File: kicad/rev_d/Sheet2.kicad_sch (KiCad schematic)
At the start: 212 parts, among them J10 vg_old, J5 external clock, J6 JUMPER, J8 JUMPER, J9 JUMPER, Q2 QUARTZ, Q3 QUARTZ32768, X10 ST-214C, X11 KEYB-MOUSE, X12 IDC20, X13 USB_C, X14 AAFP/AC97 audio, X15 PLB2-2, X16 PLB1-4I, X17 PLB1-4I, X18 PLB1-4I, X19 AVR pgm conn, X20 PLB1-4I, X21 RSA103, X4 IDC10M, X5 IDC10M, X6 RS232_9

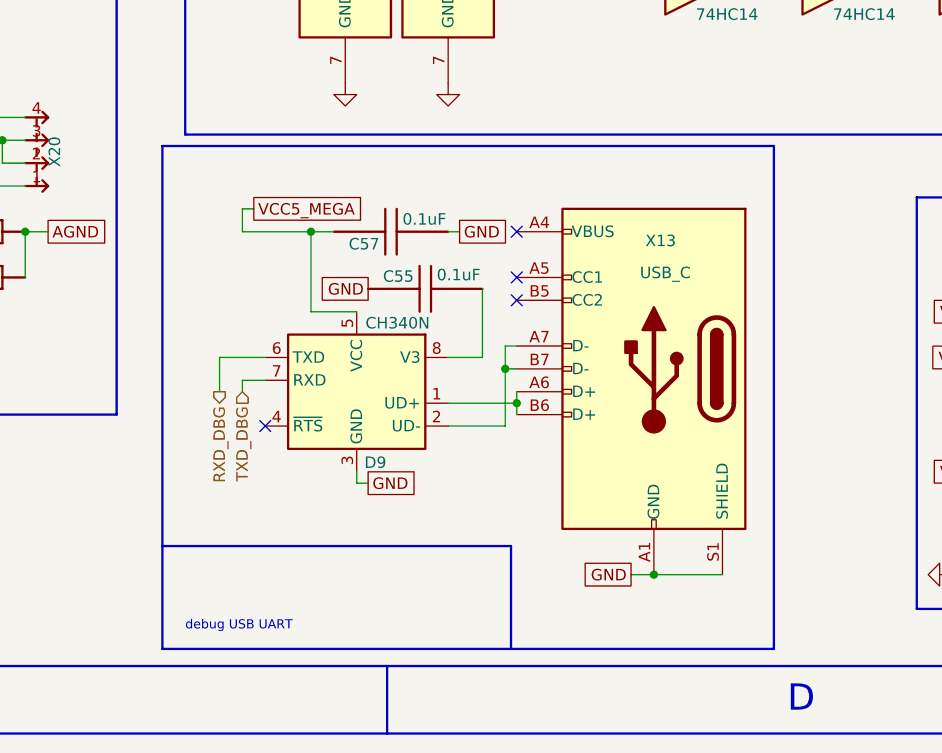
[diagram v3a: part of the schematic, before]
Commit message: pentevo: rev D: add forgotten 5k1 pulldowns for type-C CC1/CC2 pins
git-svn-id: svn://localhost/local-pentevo@1207 c6c76956-fad2-4150-a3a9-ea0a427205ba
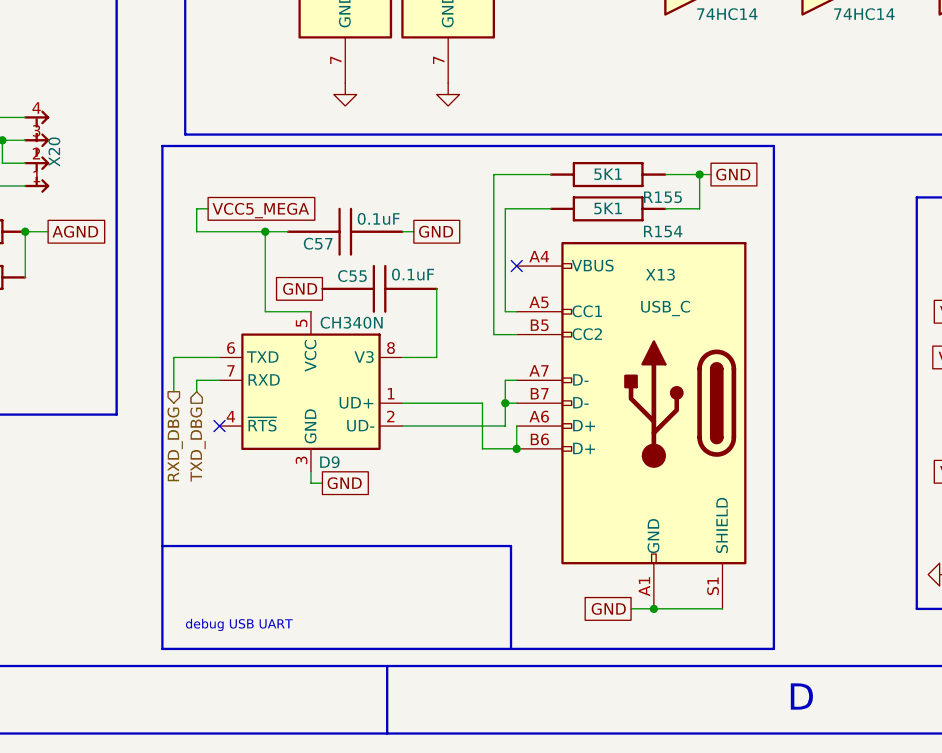
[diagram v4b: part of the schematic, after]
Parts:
- added R154, R155: 5K1, R-CHIP, symbol eva-altium-import:Sheet2_0_mirrored_RESCHIP
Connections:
- net GND: now also R154.2 (i/o1), R155.2 (i/o1)
- net at X13.A5 (CC1): now also R154.1 (i/o)
- net at X13.B5 (CC2): now also R155.1 (i/o)
- no-connect marks 31 -> 29
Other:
- moved on the sheet: C55, C57, D9, X13

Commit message: pentevo: rev D: upgrade 12v filtering, add 74hct1g04 for beep signals (much faster speed), change AVCC8 to AVCC9
git-svn-id: svn://localhost/local-pentevo@1209 c6c76956-fad2-4150-a3a9-ea0a427205ba
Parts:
- removed C12: 10uF, EC-CHIP, symbol eva-altium-import:Sheet2_3_ECAPCHIP
- removed D20: CD4069M, SO14, symbol eva-altium-import:Sheet2_0_CD4069M
- removed R99: 91, R-CHIP, symbol eva-altium-import:Sheet2_3_RESCHIP
- removed X21: RSA103, RSA103, symbol eva-altium-import:Sheet2_0_RSA103
- added C12: 0.1uF, C-CHIP, symbol eva-altium-import:Sheet2_0_CAPCHIP
- added C58, C63: 470uF, EC-CHIP, symbol eva-altium-import:Sheet2_3_ECAPCHIP
- added D20: 4069, Package_SO:SOIC-14_3.9x8.7mm_P1.27mm, symbol 4xxx:4069
- added L4: 470uH, CDR64B, symbol eva-altium-import:Sheet2_0_CDR64B
- added R156, R99: 0R5, R-CHIP, symbol eva-altium-import:Sheet2_0_RESCHIP
- added U1: 74HCT1G04, Package_TO_SOT_SMD:SOT-23-5_HandSoldering, symbol 74xGxx:74AHC1G04
- C44: value 10nF -> 1nF
- L2: value 27uH -> 470uH
- R114: value 2K2 -> 1K6
- R87: value 91 -> 150
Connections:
- net AGND: now also C44.1, C12.1, C58.2, C63.2, D20.7 (VSS), U1.3 (GND)
- net AVCC5: now also C12.2, D20.14 (VDD), U1.5 (VCC)
- net BEEP: now also D20.3, U1.2
- net TAPE_BIT: now also D20.8
- net at R95.1 (i/o): now also D20.10, D20.9
- net at C14.1, C15.1, DA2.1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: now also R87.1 (i/o)
- net at R164.2 (i/o1): now also D20.4
- net at R95.2 (i/o1), VD7.2 (C), VD8.1 (A): now also D20.11, D20.12
- net AVCC12: now reaches C10.1, C35.1, DA2.3 (in), DA5.1 (in), VD18.1 (K), VD19.1 (K)
- net AVCC12: now also C63.1, R156.2 (i/o1); no longer L2.1
- net at R94.1 (i/o), VD7.1 (A), VD8.2 (C): now also D20.13
- net at R114.2 (i/o1): now also U1.4
- net AVCC8 renamed AVCC9
- net AVCC9: no longer C44.1
- new net: C58.1, L4.1, R99.1 (i/o)
- new net: L2.1, R99.2 (i/o1)
- new net: D20.1, D20.6
- new net: D20.2, D20.5
- new net: L4.2, R156.1 (i/o)
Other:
- note added: "alt. supervisor is KA75450"
- moved on the sheet: C10, C105, C11, C13, C14, C15, C29, C33, C35, C37, DA2, R87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

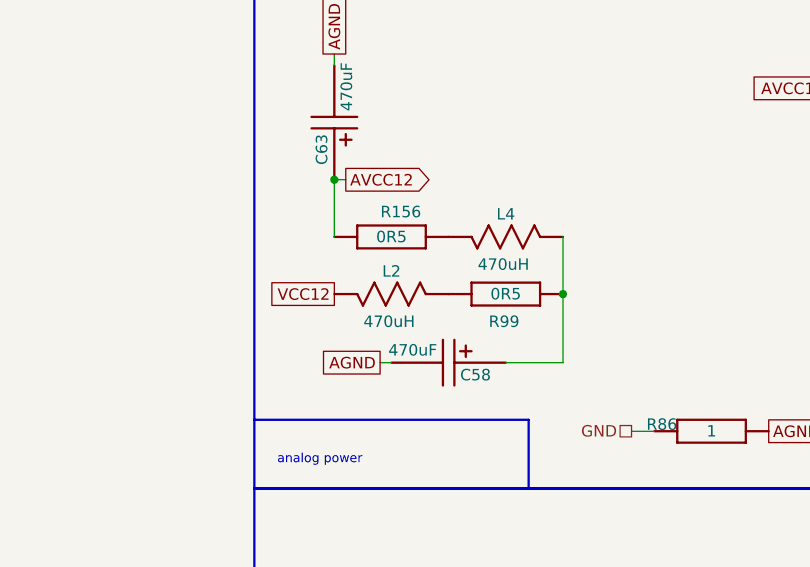
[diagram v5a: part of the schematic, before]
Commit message: pentevo: rev D: update footprints for 470uF and 470uH, remove 0R5 resistors
git-svn-id: svn://localhost/local-pentevo@1210 c6c76956-fad2-4150-a3a9-ea0a427205ba
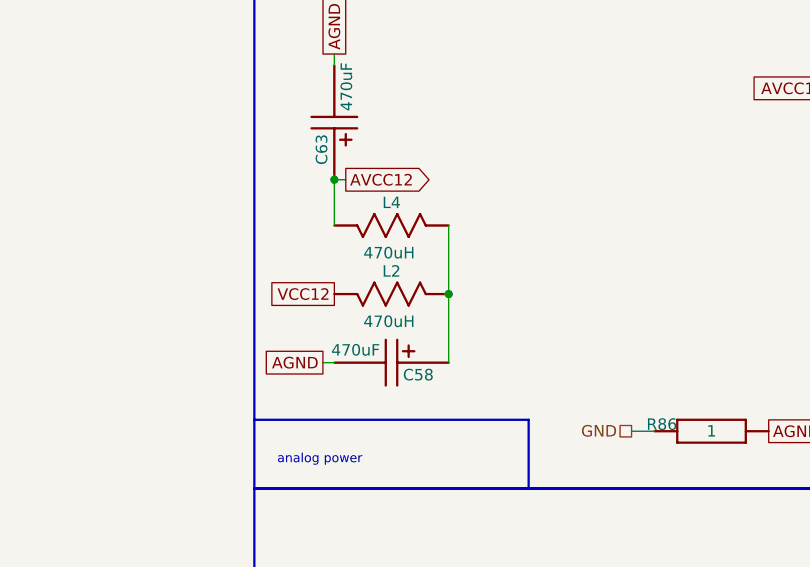
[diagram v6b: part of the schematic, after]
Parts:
- removed R156, R99: 0R5, R-CHIP, symbol eva-altium-import:Sheet2_0_RESCHIP
- C58, C63: footprint EC-CHIP -> Capacitor_THT:CP_Radial_D10.0mm_P5.00mm
- L2, L4: footprint CDR64B -> Inductor_SMD:L_Bourns_SRP6060FA
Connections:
- net AVCC12: now also L4.2
- net at C58.1, L4.1: now also L2.1
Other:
- moved on the sheet: C58, L4
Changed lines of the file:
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@@
 	)
 	(junction
-		(at 115.57 257.81)
-		(diameter 0)
-		(color 0 0 0 0)
-	)
-	(junction
 		(at 384.81 85.09)
 		(diameter 0)
@@
 	)
 	(junction
+		(at 102.87 257.81)
+		(diameter 0)
+		(color 0 0 0 0)
+	)
+	(junction
 		(at 147.32 335.28)
 		(diameter 0)
@@
 	(wire
 		(pts
+			(xy 102.87 250.19) (xy 102.87 257.81)
+		)
+		(stroke
+			(width 0)
+			(type default)
+		)
+	)
+	(wire
+		(pts
 			(xy 297.18 195.58) (xy 330.2 195.58)
 		)
@@
 	(wire
 		(pts
-			(xy 115.57 265.43) (xy 109.22 265.43)
-		)
-		(stroke
-			(width 0)
-			(type default)
-		)
-	)
-	(wire
-		(pts
 			(xy 93.98 347.98) (xy 93.98 353.06)
 		)
@@
 		)
 	)
-	(wire
-		(pts
-			(xy 115.57 251.46) (xy 115.57 257.81)
-		)
-		(stroke
-			(width 0)
-			(type default)
-		)
-	)
 	(polyline
 		(pts
@@
 	(wire
 		(pts
+			(xy 102.87 257.81) (xy 102.87 265.43)
+		)
+		(stroke
+			(width 0)
+			(type default)
+		)
+	)
+	(wire
+		(pts
 			(xy 218.44 71.12) (xy 218.44 63.5)
 		)
@@
 	(wire
 		(pts
-			(xy 90.17 245.11) (xy 90.17 251.46)
+			(xy 90.17 245.11) (xy 90.17 250.19)
 		)
 		(stroke
@@
 	(wire
 		(pts
-			(xy 95.25 265.43) (xy 96.52 265.43)
+			(xy 88.9 265.43) (xy 90.17 265.43)
 		)
 		(stroke
@@
 	(wire
 		(pts
-			(xy 115.57 257.81) (xy 115.57 265.43)
-		)
-		(stroke
-			(width 0)
-			(type default)
-		)
-	)
-	(wire
-		(pts
 			(xy 180.34 234.95) (xy 185.42 234.95)
 		)
@@
 	(global_label "AGND"
 		(shape passive)
-		(at 95.25 265.43 180)
+		(at 88.9 265.43 180)
 		(fields_autoplaced yes)
 		(effects
@@
 		)
 		(property "Intersheetrefs" "${INTERSHEET_REFS}"
-			(at 88.417 265.43 0)
+			(at 82.067 265.43 0)
 			(effects
 				(font
@@
 			)
 		)
-		(property "Footprint" "EC-CHIP"
+		(property "Footprint" "Capacitor_THT:CP_Radial_D10.0mm_P5.00mm"
 			(at 90.17 245.11 0)
 			(effects
@@
 	)
 	(symbol
-		(lib_id "eva-altium-import:Sheet2_0_RESCHIP")
-		(at 102.87 257.81 0)
-		(unit 1)
-		(exclude_from_sim no)
-		(in_bom yes)
-		(on_board yes)
-		(dnp no)
-		(property "Reference" "R99"
-			(at 110.744 261.62 0)
-			(effects
-				(font
-					(size 1.27 1.27)
-				)
-				(justify right bottom)
-			)
-		)
-		(property "Value" "0R5"
-			(at 109.22 257.81 0)
-			(effects
-				(font
-					(size 1.27 1.27)
-				)
-			)
-		)
-		(property "Footprint" "R-CHIP"
-			(at 102.87 257.81 0)
-			(effects
-				(font
-					(size 1.27 1.27)
-				)
-				(hide yes)
-			)
-		)
-		(property "Datasheet" ""
-			(at 102.87 257.81 0)
-			(effects
-				(font
-					(size 1.27 1.27)
-				)
-				(hide yes)
-			)
-		)
-		(property "Description" "RESCHIP"
-			(at 102.87 257.81 0)
-			(effects
-				(font
-					(size 1.27 1.27)
-				)
-				(hide yes)
-			)
-		)
-		(pin "2"
-		)
-		(pin "1"
-		)
-		(instances
-			(project "eva"
-				(path "/ab605654-a730-497b-9e09-9b351f74b935/31d5864f-06ec-4c73-9256-780a6880087d"
-					(reference "R99")
-					(unit 1)
-				)
-			)
-		)
-	)
-	(symbol
 		(lib_id "power:GND")
 		(at 366.395 375.92 0)
@@
 	(symbol
 		(lib_id "eva-altium-import:Sheet2_3_ECAPCHIP")
-		(at 109.22 265.43 270)
+		(at 102.87 265.43 270)
 		(unit 1)
 		(exclude_from_sim no)
@@
 		(dnp no)
 		(property "Reference" "C58"
-			(at 104.14 266.065 90)
+			(at 97.79 266.065 90)
 			(effects
 				(font
@@
 		)
 		(property "Value" "470uF"
-			(at 101.6 264.795 90)
+			(at 95.25 264.795 90)
 			(effects
 				(font
@@
 			)
 		)
-		(property "Footprint" "EC-CHIP"
-			(at 109.22 265.43 0)
+		(property "Footprint" "Capacitor_THT:CP_Radial_D10.0mm_P5.00mm"
+			(at 102.87 265.43 0)
 			(effects
 				(font
@@
 		)
 		(property "Datasheet" ""
-			(at 109.22 265.43 0)
+			(at 102.87 265.43 0)
 			(effects
 				(font
@@
 		)
 		(property "Description" "ECAPCHIP"
-			(at 109.22 265.43 0)
+			(at 102.87 265.43 0)
 			(effects
 				(font
@@
 	(symbol
 		(lib_id "eva-altium-import:Sheet2_0_CDR64B")
-		(at 102.87 251.46 0)
+		(at 90.17 250.19 0)
 		(unit 1)
 		(exclude_from_sim no)
@@
 		(dnp no)
 		(property "Reference" "L4"
-			(at 109.22 249.682 0)
+			(at 96.52 248.412 0)
 			(effects
 				(font
@@
 		)
 		(property "Value" "470uH"
-			(at 108.966 255.27 0)
+			(at 96.266 254 0)
 			(effects
 				(font
@@
 			)
 		)
-		(property "Footprint" "CDR64B"
-			(at 102.87 251.46 0)
+		(property "Footprint" "Inductor_SMD:L_Bourns_SRP6060FA"
+			(at 90.17 250.19 0)
 			(effects
 				(font
@@
 		)
 		(property "Datasheet" ""
-			(at 102.87 251.46 0)
+			(at 90.17 250.19 0)
 			(effects
 				(font
@@
 		)
 		(property "Description" "CDR64B"
-			(at 102.87 251.46 0)
+			(at 90.17 250.19 0)
 			(effects
 				(font
@@
 			)
 		)
-		(property "Footprint" "CDR64B"
+		(property "Footprint" "Inductor_SMD:L_Bourns_SRP6060FA"
 			(at 90.17 257.81 0)
 			(effects
@@
 					(unit 1)
 				)
-			)
-		)
-	)
-	(symbol
-		(lib_id "eva-altium-import:Sheet2_0_RESCHIP")
-		(at 90.17 251.46 0)
-		(unit 1)
-		(exclude_from_sim no)
-		(in_bom yes)
-		(on_board yes)
-		(dnp no)
-		(property "Reference" "R156"
-			(at 99.822 249.428 0)
-			(effects
-				(font
-					(size 1.27 1.27)
-				)
-				(justify right bottom)
-			)
-		)
-		(property "Value" "0R5"
-			(at 96.52 251.46 0)
-			(effects
-				(font
-					(size 1.27 1.27)
-				)
-			)
-		)
-		(property "Footprint" "R-CHIP"
-			(at 90.17 251.46 0)
-			(effects
-				(font
-					(size 1.27 1.27)
-				)
-				(hide yes)
-			)
-		)
-		(property "Datasheet" ""
-			(at 90.17 251.46 0)
-			(effects
-				(font
-					(size 1.27 1.27)
-				)
-				(hide yes)
-			)
-		)
-		(property "Description" "RESCHIP"
-			(at 90.17 251.46 0)
-			(effects
-				(font
-					(size 1.27 1.27)
-				)
-				(hide yes)
-			)
-		)
-		(pin "2"
-		)
-		(pin "1"
-		)
-		(instances
-			(project "eva"
-				(path "/ab605654-a730-497b-9e09-9b351f74b935/31d5864f-06ec-4c73-9256-780a6880087d"
-					(reference "R156")
-					(unit 1)
-				)
